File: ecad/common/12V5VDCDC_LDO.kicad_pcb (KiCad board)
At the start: 2 copper layers, 11 parts, among them U4 MIC4680YM

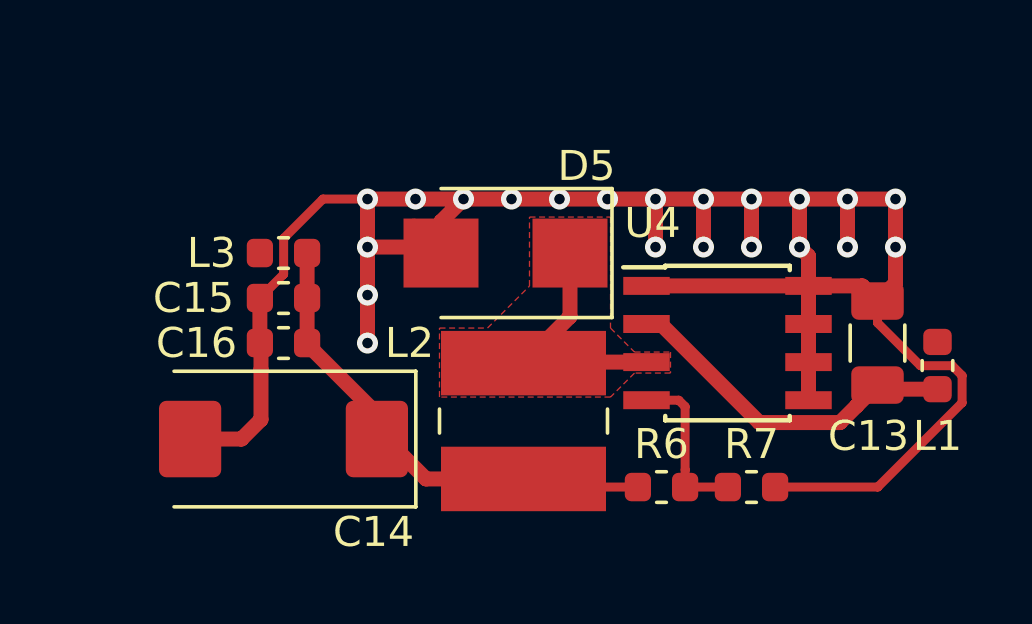
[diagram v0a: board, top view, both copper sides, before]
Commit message: Updates coomon design file with KiCad 5 defaults
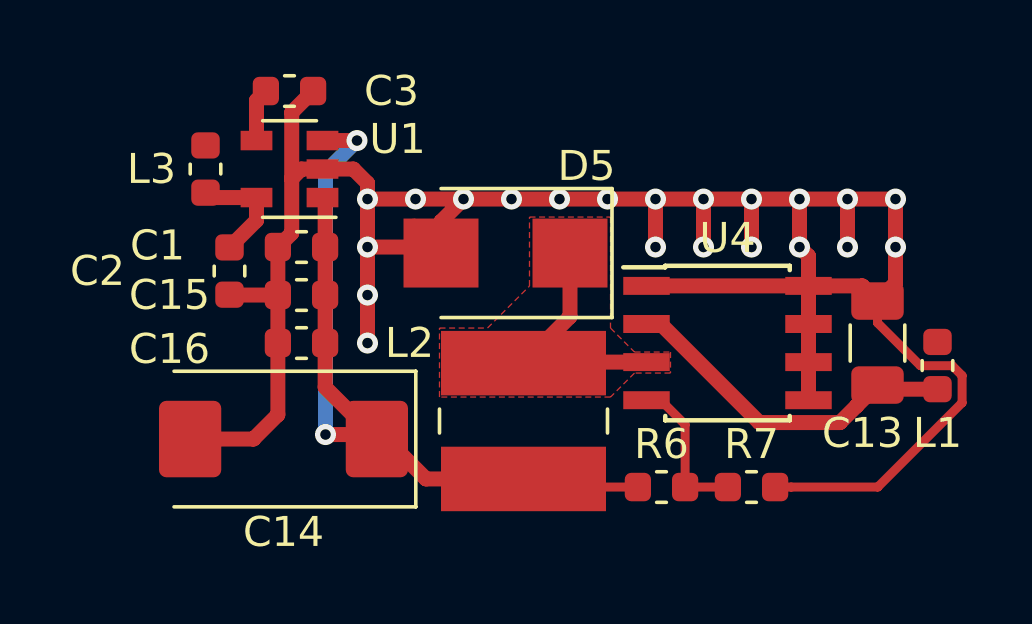
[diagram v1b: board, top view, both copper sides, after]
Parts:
- added C1: 1u, Capacitor_SMD:C_0603_1608Metric, F.Cu at (133.8, 96.8)
- added C2: 1u, Capacitor_SMD:C_0603_1608Metric, F.Cu at (131.4, 97.6)
- added C3: 10n, Capacitor_SMD:C_0603_1608Metric, F.Cu at (133.4, 91.6)
- added U1: LP3985IM5-5.0_NOPB, Package_TO_SOT_SMD:SOT-23-5, F.Cu at (133.4, 94.2)
- R7: value 4k7 -> 4k32
- moved L3 3.82 mm to (130.6, 94.2), turned to 270 degrees
- moved C15 0.61 mm to (133.8, 98.4)
- moved C16 0.60 mm to (133.8, 100.0)
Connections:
- C14 pad 1: /5V_UNPROTECTED -> /5V5_UNPROTECTED
- C15 pad 1: /5V_UNPROTECTED -> /5V5_UNPROTECTED
- C16 pad 1: /5V_UNPROTECTED -> /5V5_UNPROTECTED
- L2 pad 2: /5V_UNPROTECTED -> /5V5_UNPROTECTED
- R6 pad 1: /5V_UNPROTECTED -> /5V5_UNPROTECTED
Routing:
- net /5V5_UNPROTECTED: track 0.00 -> 31.6 mm, vias 0 -> 2
- net /5V_UNPROTECTED: track 16.8 -> 3.80 mm
- net GND: track 78.2 -> 85.3 mm
- net Net-(C3-Pad1): track 0.00 -> 1.78 mm
